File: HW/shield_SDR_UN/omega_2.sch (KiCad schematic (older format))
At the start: 15 parts

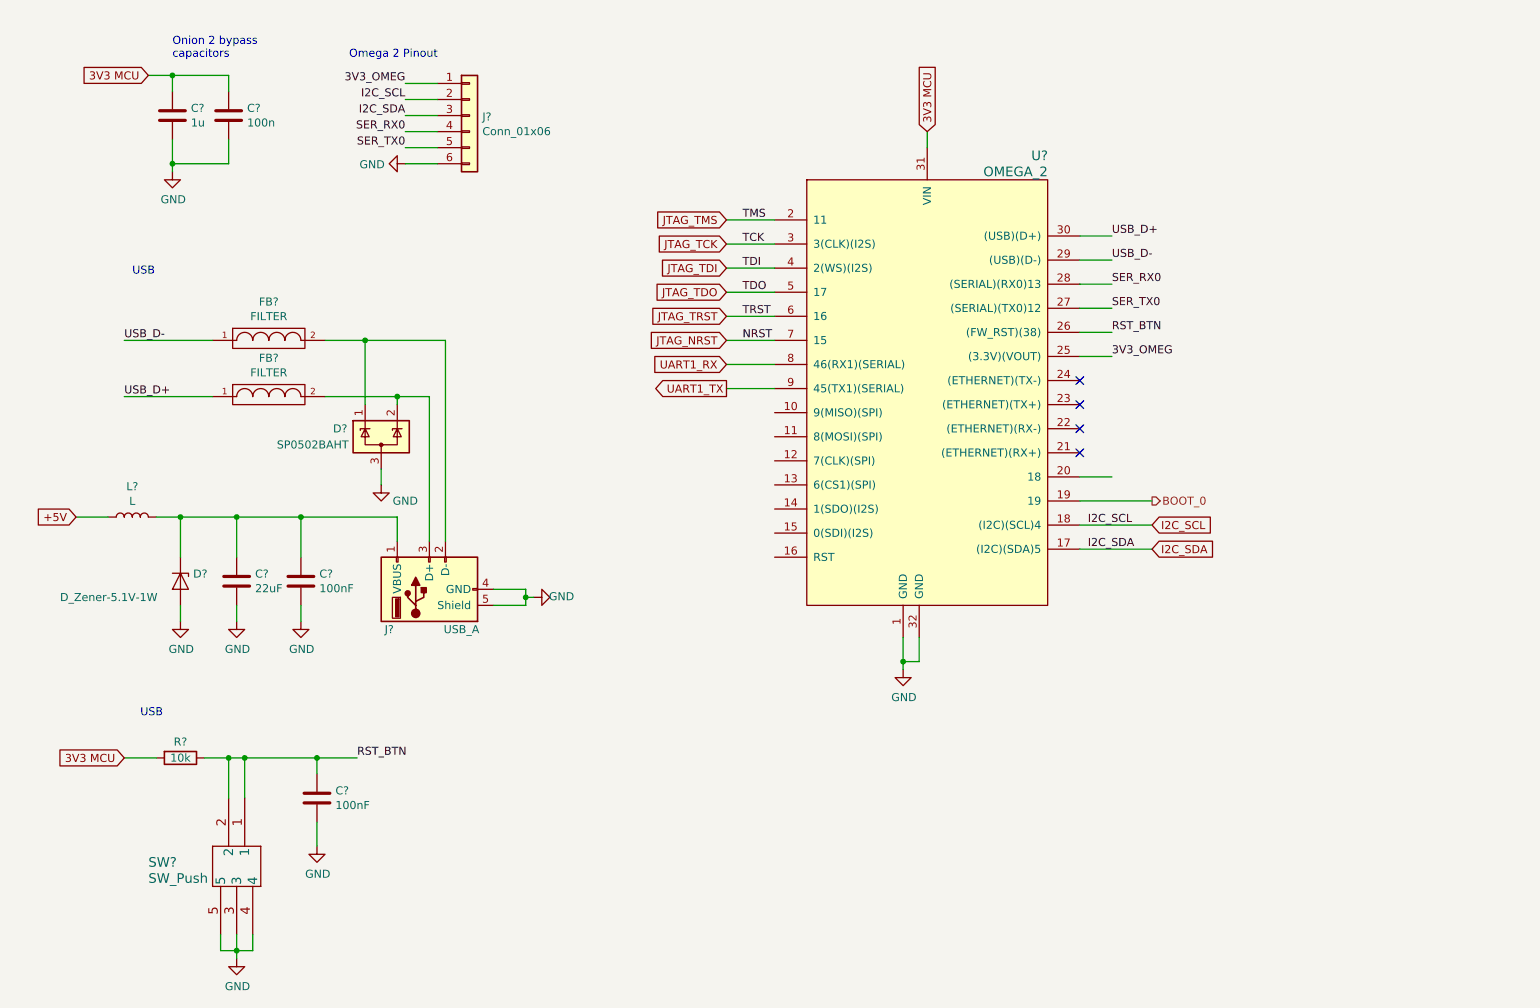
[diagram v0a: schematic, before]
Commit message: STM32 connection updated
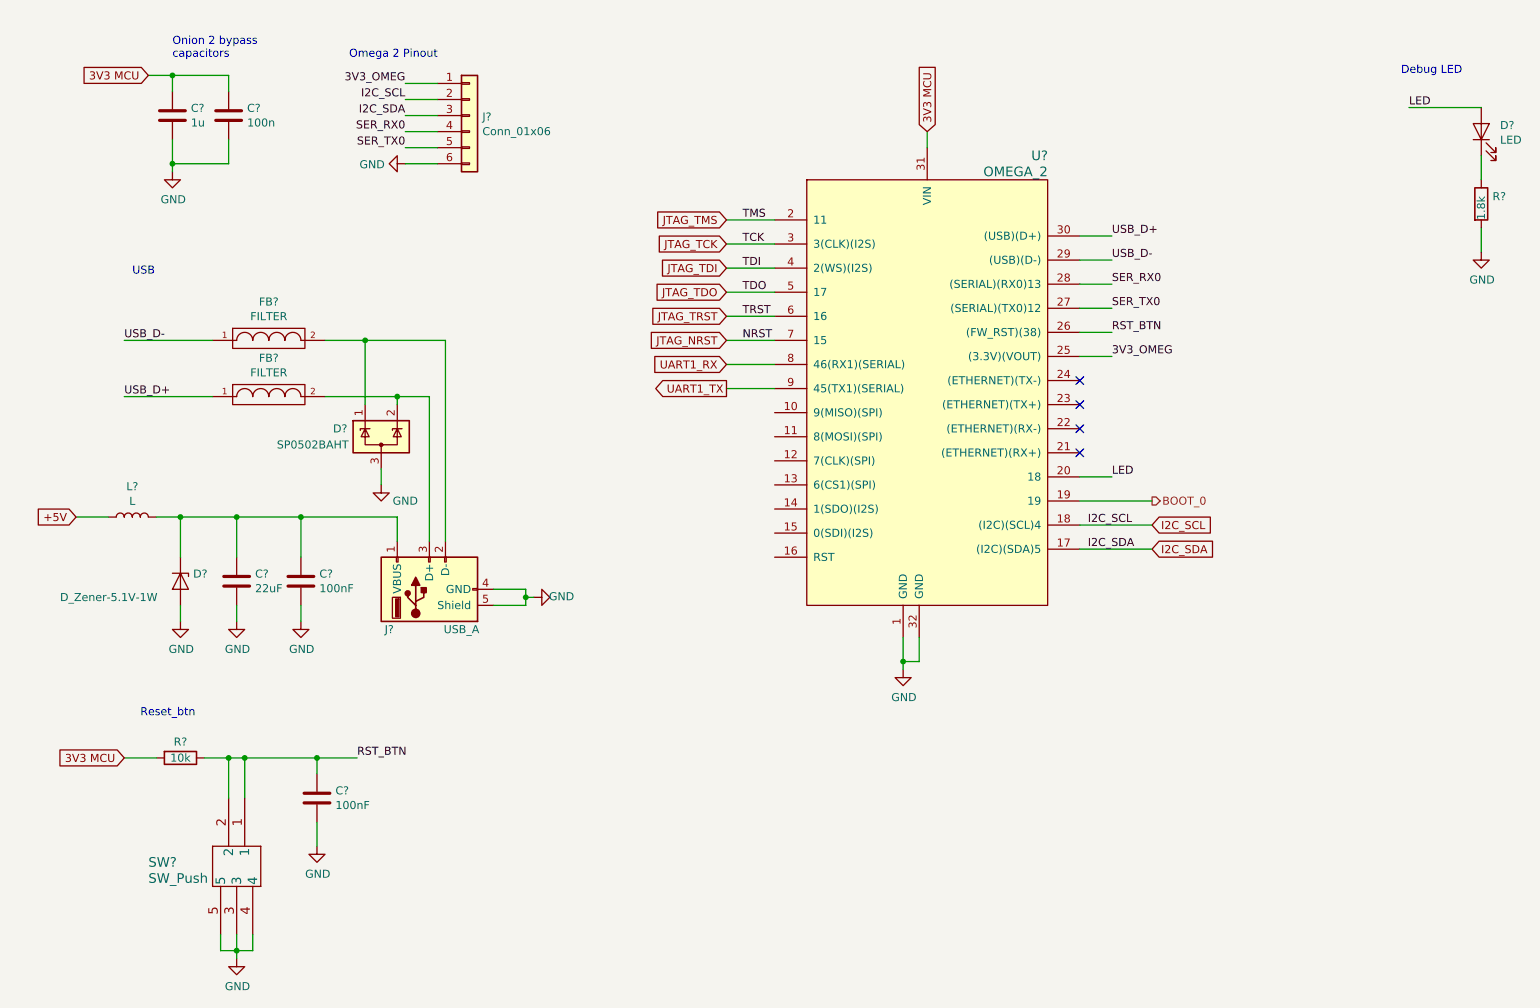
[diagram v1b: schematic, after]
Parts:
- added D?: LED, symbol Device:LED
- added R?: 1.8k, symbol Device:R
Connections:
- net GND: now also R?.2
- net LED: now reaches U?.20 (18)
- net LED: now also D?.2 (A)
- new net: D?.1 (K), R?.1
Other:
- note added: "Debug LED"
- note added: "Reset_btn"
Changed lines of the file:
@@
 RST_BTN
 Text Notes 1300 5050 0    50   ~ 0
-USB
+Reset_btn
 Wire Wire Line
 	5250 1950 4950 1950
@@
 Wire Wire Line
 	5250 3000 4950 3000
+$Comp
+L Device:LED D?
+U 1 1 5D35F1A3
+P 9650 1400
+AR Path="/5CC082AD/5D35F1A3" Ref="D?"  Part="1"
+AR Path="/5CFB52DC/5D35F1A3" Ref="D?"  Part="1"
+F 0 "D?" V 9689 1283 50  0000 R CNN
+F 1 "LED" V 9598 1283 50  0000 R CNN
+F 2 "" H 9650 1400 50  0001 C CNN
+F 3 "~" H 9650 1400 50  0001 C CNN
+	1    9650 1400
+	0    -1   -1   0
+$EndComp
+$Comp
+L Device:R R?
+U 1 1 5D35F1AD
+P 9650 1850
+AR Path="/5CC082AD/5D35F1AD" Ref="R?"  Part="1"
+AR Path="/5CFB52DC/5D35F1AD" Ref="R?"  Part="1"
+F 0 "R?" H 9720 1896 50  0000 L CNN
+F 1 "1.8k" V 9650 1750 50  0000 L CNN
+F 2 "" V 9580 1850 50  0001 C CNN
+F 3 "~" H 9650 1850 50  0001 C CNN
+	1    9650 1850
+	1    0    0    -1
+$EndComp
+$Comp
+L power:GND #PWR?
+U 1 1 5D35F1B5
+P 9650 2150
+F 0 "#PWR?" H 9650 1900 50  0001 C CNN
+F 1 "GND" H 9655 1977 50  0000 C CNN
+F 2 "" H 9650 2150 50  0001 C CNN
+F 3 "" H 9650 2150 50  0001 C CNN
+	1    9650 2150
+	1    0    0    -1
+$EndComp
+Wire Wire Line
+	9650 1250 9200 1250
+Wire Wire Line
+	9650 1550 9650 1700
+Wire Wire Line
+	9650 2000 9650 2150
+Text Label 9200 1250 0    50   ~ 0
+LED
+Text Notes 9150 1050 0    50   ~ 0
+Debug LED
+Text Label 7350 3550 0    50   ~ 0
+LED
 $EndSCHEMATC

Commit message: algunos footprint
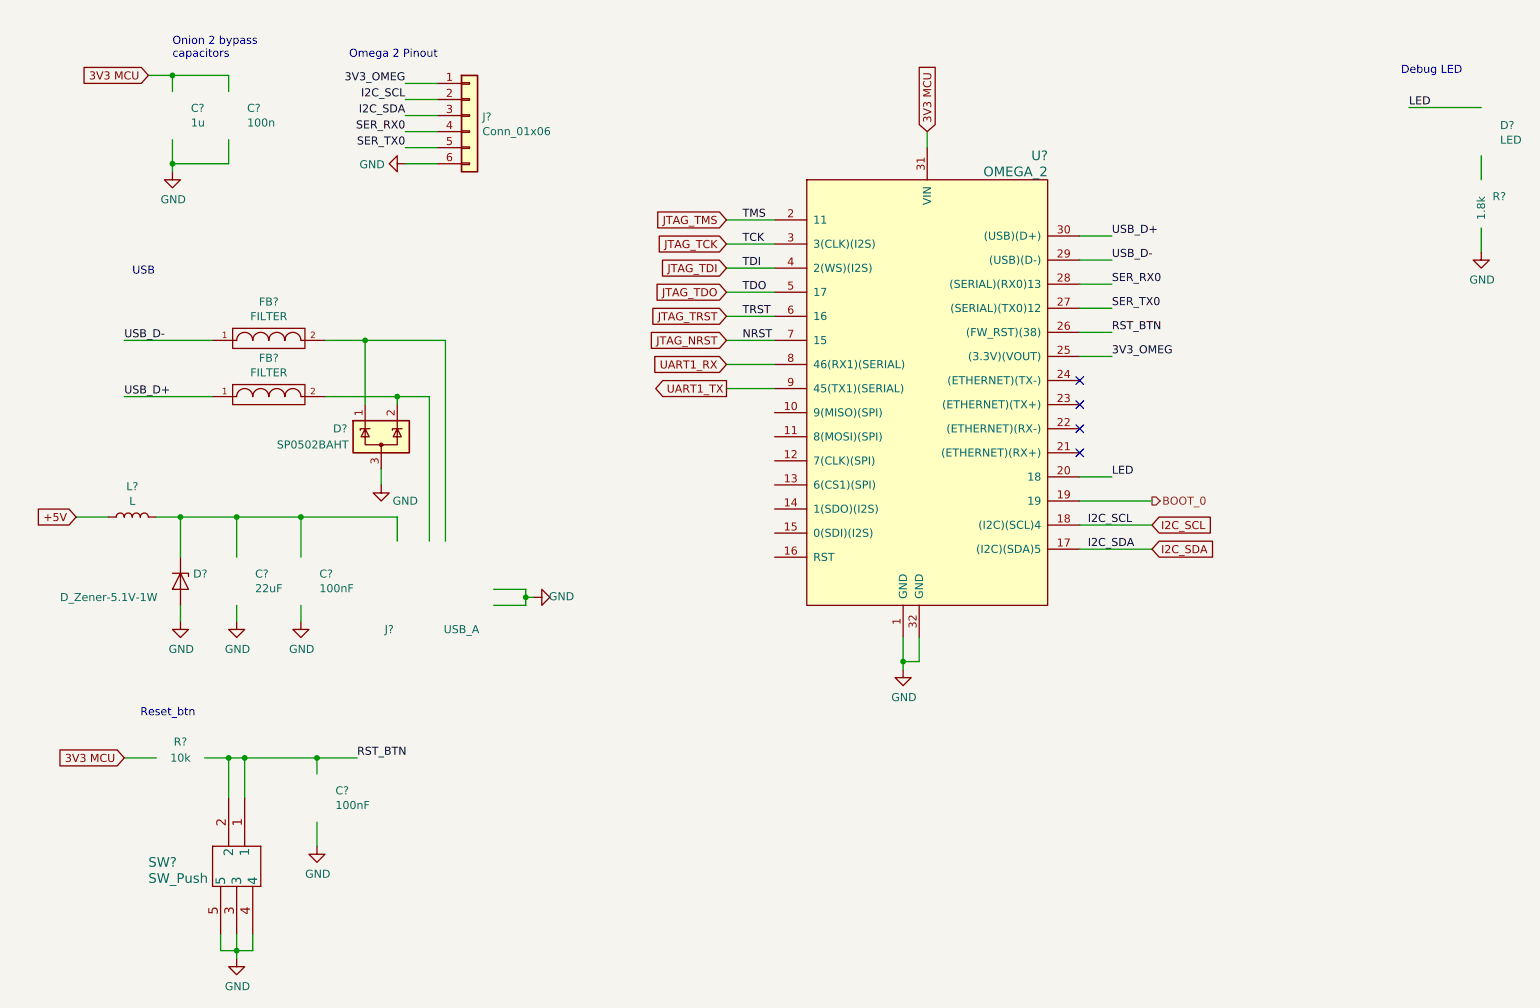
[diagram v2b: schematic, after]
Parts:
- C? (x2): footprint (none) -> Capacitor_SMD:C_0402_1005Metric
- D?: footprint (none) -> LED_SMD:LED_0805_2012Metric_Pad1.15x1.40mm_HandSolder
- J?: footprint (none) -> Connector_USB:USB_Micro-B_GCT_USB3076-30-A
- R? (x2): footprint (none) -> Resistor_SMD:R_0603_1608Metric_Pad1.05x0.95mm_HandSolder
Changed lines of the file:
@@
 $EndComp
 $Comp
-L power:GND #PWR?
+L power:GND #PWR0193
 U 1 1 5CE0713A
 P 6050 4750
-F 0 "#PWR?" H 6050 4500 50  0001 C CNN
+F 0 "#PWR0193" H 6050 4500 50  0001 C CNN
 F 1 "GND" H 6055 4577 50  0000 C CNN
 F 2 "" H 6050 4750 50  0001 C CNN
@@
 $Comp
 L Device:C C?
-U 1 1 5CE14EC4
+U 0 0 5CE14EC4
 P 1500 1300
 F 0 "C?" H 1615 1346 50  0000 L CNN
 F 1 "1u" H 1615 1255 50  0000 L CNN
-F 2 "" H 1538 1150 50  0001 C CNN
+F 2 "Capacitor_SMD:C_0402_1005Metric" H 1538 1150 50  0001 C CNN
 F 3 "~" H 1500 1300 50  0001 C CNN
-	1    1500 1300
+	0    1500 1300
 	1    0    0    -1
 $EndComp
 $Comp
 L Device:C C?
-U 1 1 5CE15558
+U 0 0 5CE15558
 P 1850 1300
 F 0 "C?" H 1965 1346 50  0000 L CNN
 F 1 "100n" H 1965 1255 50  0000 L CNN
-F 2 "" H 1888 1150 50  0001 C CNN
+F 2 "Capacitor_SMD:C_0402_1005Metric" H 1888 1150 50  0001 C CNN
 F 3 "~" H 1850 1300 50  0001 C CNN
-	1    1850 1300
-	1    0    0    -1
-$EndComp
-$Comp
-L power:GND #PWR?
+	0    1850 1300
+	1    0    0    -1
+$EndComp
+$Comp
+L power:GND #PWR0194
 U 1 1 5CE166D1
 P 1500 1650
-F 0 "#PWR?" H 1500 1400 50  0001 C CNN
+F 0 "#PWR0194" H 1500 1400 50  0001 C CNN
 F 1 "GND" H 1505 1477 50  0000 C CNN
 F 2 "" H 1500 1650 50  0001 C CNN
@@
 $Comp
 L Device:C C?
-U 1 1 5CECC457
+U 0 0 5CECC457
 P 1900 4200
 AR Path="/5CC08321/5CECC457" Ref="C?"  Part="1"
-AR Path="/5CFB52DC/5CECC457" Ref="C?"  Part="1"
+AR Path="/5CFB52DC/5CECC457" Ref="C?"  Part="0"
 F 0 "C?" H 2015 4246 50  0000 L CNN
 F 1 "22uF" H 2015 4155 50  0000 L CNN
 F 2 "modules:C_0805_HandSoldering" H 1938 4050 50  0001 C CNN
 F 3 "~" H 1900 4200 50  0001 C CNN
-	1    1900 4200
+	0    1900 4200
 	1    0    0    -1
 $EndComp
@@
 	3700 4250 3500 4250
 $Comp
-L power:GND #PWR?
+L power:GND #PWR0195
 U 1 1 5CECC493
 P 3750 4300
-F 0 "#PWR?" H 3750 4050 50  0001 C CNN
+F 0 "#PWR0195" H 3750 4050 50  0001 C CNN
 F 1 "GND" V 3755 4127 50  0000 C CNN
 F 2 "" H 3750 4300 50  0001 C CNN
@@
 $Comp
 L Device:C C?
-U 1 1 5CECC461
+U 0 0 5CECC461
 P 2300 4200
 AR Path="/5CC08321/5CECC461" Ref="C?"  Part="1"
-AR Path="/5CFB52DC/5CECC461" Ref="C?"  Part="1"
+AR Path="/5CFB52DC/5CECC461" Ref="C?"  Part="0"
 F 0 "C?" H 2415 4246 50  0000 L CNN
 F 1 "100nF" H 2415 4155 50  0000 L CNN
 F 2 "Capacitor_SMD:C_0402_1005Metric" H 2338 4050 50  0001 C CNN
 F 3 "~" H 2300 4200 50  0001 C CNN
-	1    2300 4200
-	1    0    0    -1
-$EndComp
-$Comp
-L power:GND #PWR?
+	0    2300 4200
+	1    0    0    -1
+$EndComp
+$Comp
+L power:GND #PWR0196
 U 1 1 5CF38DF9
 P 1900 4450
-F 0 "#PWR?" H 1900 4200 50  0001 C CNN
+F 0 "#PWR0196" H 1900 4200 50  0001 C CNN
 F 1 "GND" H 1905 4277 50  0000 C CNN
 F 2 "" H 1900 4450 50  0001 C CNN
@@
 $EndComp
 $Comp
-L power:GND #PWR?
+L power:GND #PWR0197
 U 1 1 5CF3BDF7
 P 2300 4450
-F 0 "#PWR?" H 2300 4200 50  0001 C CNN
+F 0 "#PWR0197" H 2300 4200 50  0001 C CNN
 F 1 "GND" H 2305 4277 50  0000 C CNN
 F 2 "" H 2300 4450 50  0001 C CNN
@@
 $EndComp
 $Comp
-L power:GND #PWR?
+L power:GND #PWR0198
 U 1 1 5CF3C29A
 P 1550 4450
-F 0 "#PWR?" H 1550 4200 50  0001 C CNN
+F 0 "#PWR0198" H 1550 4200 50  0001 C CNN
 F 1 "GND" H 1555 4277 50  0000 C CNN
 F 2 "" H 1550 4450 50  0001 C CNN
@@
 $Comp
 L Connector:USB_A J?
-U 1 1 5CECC443
+U 0 0 5CECC443
 P 3100 4250
 AR Path="/5CC08321/5CECC443" Ref="J?"  Part="1"
-AR Path="/5CFB52DC/5CECC443" Ref="J?"  Part="1"
+AR Path="/5CFB52DC/5CECC443" Ref="J?"  Part="0"
 F 0 "J?" V 2850 4500 50  0000 C CNN
 F 1 "USB_A" V 2850 4050 50  0000 C CNN
-F 2 "" H 3250 4200 50  0001 C CNN
+F 2 "Connector_USB:USB_Micro-B_GCT_USB3076-30-A" H 3250 4200 50  0001 C CNN
 F 3 "" H 3250 4200 50  0001 C CNN
 F 4 "https://www.digikey.com/product-detail/en/amphenol-icc-commercial-products/UE27AC54100/UE27AC54100-ND/1972253" H 3100 4250 50  0001 C CNN "digikey"
-	1    3100 4250
+	0    3100 4250
 	0    -1   -1   0
 $EndComp
@@
 $EndComp
 $Comp
-L power:GND #PWR?
+L power:GND #PWR0199
 U 1 1 5CF9308C
 P 2800 3600
-F 0 "#PWR?" H 2800 3350 50  0001 C CNN
+F 0 "#PWR0199" H 2800 3350 50  0001 C CNN
 F 1 "GND" H 2950 3500 50  0000 C CNN
 F 2 "" H 2800 3600 50  0001 C CNN
@@
 3V3_OMEG
 $Comp
-L power:GND #PWR?
+L power:GND #PWR0200
 U 1 1 5D026364
 P 2950 1600
-F 0 "#PWR?" H 2950 1350 50  0001 C CNN
+F 0 "#PWR0200" H 2950 1350 50  0001 C CNN
 F 1 "GND" V 2955 1472 50  0000 R CNN
 F 2 "" H 2950 1600 50  0001 C CNN
@@
 $Comp
 L Device:R R?
-U 1 1 5CD67141
+U 0 0 5CD67141
 P 1550 5300
 F 0 "R?" V 1450 5300 50  0000 C CNN
 F 1 "10k" V 1550 5300 50  0000 C CNN
-F 2 "" V 1480 5300 50  0001 C CNN
+F 2 "Resistor_SMD:R_0603_1608Metric_Pad1.05x0.95mm_HandSolder" V 1480 5300 50  0001 C CNN
 F 3 "~" H 1550 5300 50  0001 C CNN
-	1    1550 5300
+	0    1550 5300
 	0    1    1    0
 $EndComp
@@
 	1400 5300 1200 5300
 $Comp
-L power:GND #PWR?
+L power:GND #PWR0201
 U 1 1 5CD80A5F
 P 1900 6550
-F 0 "#PWR?" H 1900 6300 50  0001 C CNN
+F 0 "#PWR0201" H 1900 6300 50  0001 C CNN
 F 1 "GND" H 1905 6377 50  0000 C CNN
 F 2 "" H 1900 6550 50  0001 C CNN
@@
 $Comp
 L Device:C C?
-U 1 1 5CD83476
+U 0 0 5CD83476
 P 2400 5550
 AR Path="/5CC08321/5CD83476" Ref="C?"  Part="1"
-AR Path="/5CFB52DC/5CD83476" Ref="C?"  Part="1"
+AR Path="/5CFB52DC/5CD83476" Ref="C?"  Part="0"
 F 0 "C?" H 2515 5596 50  0000 L CNN
 F 1 "100nF" H 2515 5505 50  0000 L CNN
 F 2 "Capacitor_SMD:C_0402_1005Metric" H 2438 5400 50  0001 C CNN
 F 3 "~" H 2400 5550 50  0001 C CNN
-	1    2400 5550
-	1    0    0    -1
-$EndComp
-$Comp
-L power:GND #PWR?
+	0    2400 5550
+	1    0    0    -1
+$EndComp
+$Comp
+L power:GND #PWR0202
 U 1 1 5CD83F6F
 P 2400 5850
-F 0 "#PWR?" H 2400 5600 50  0001 C CNN
+F 0 "#PWR0202" H 2400 5600 50  0001 C CNN
 F 1 "GND" H 2405 5677 50  0000 C CNN
 F 2 "" H 2400 5850 50  0001 C CNN
@@
 $Comp
 L Device:LED D?
-U 1 1 5D35F1A3
+U 0 0 5D35F1A3
 P 9650 1400
 AR Path="/5CC082AD/5D35F1A3" Ref="D?"  Part="1"
-AR Path="/5CFB52DC/5D35F1A3" Ref="D?"  Part="1"
+AR Path="/5CFB52DC/5D35F1A3" Ref="D?"  Part="0"
 F 0 "D?" V 9689 1283 50  0000 R CNN
 F 1 "LED" V 9598 1283 50  0000 R CNN
-F 2 "" H 9650 1400 50  0001 C CNN
+F 2 "LED_SMD:LED_0805_2012Metric_Pad1.15x1.40mm_HandSolder" H 9650 1400 50  0001 C CNN
 F 3 "~" H 9650 1400 50  0001 C CNN
-	1    9650 1400
+	0    9650 1400
 	0    -1   -1   0
 $EndComp
 $Comp
 L Device:R R?
-U 1 1 5D35F1AD
+U 0 0 5D35F1AD
 P 9650 1850
 AR Path="/5CC082AD/5D35F1AD" Ref="R?"  Part="1"
-AR Path="/5CFB52DC/5D35F1AD" Ref="R?"  Part="1"
+AR Path="/5CFB52DC/5D35F1AD" Ref="R?"  Part="0"
 F 0 "R?" H 9720 1896 50  0000 L CNN
 F 1 "1.8k" V 9650 1750 50  0000 L CNN
-F 2 "" V 9580 1850 50  0001 C CNN
+F 2 "Resistor_SMD:R_0603_1608Metric_Pad1.05x0.95mm_HandSolder" V 9580 1850 50  0001 C CNN
 F 3 "~" H 9650 1850 50  0001 C CNN
-	1    9650 1850
-	1    0    0    -1
-$EndComp
-$Comp
-L power:GND #PWR?
+	0    9650 1850
+	1    0    0    -1
+$EndComp
+$Comp
+L power:GND #PWR0203
 U 1 1 5D35F1B5
 P 9650 2150
-F 0 "#PWR?" H 9650 1900 50  0001 C CNN
+F 0 "#PWR0203" H 9650 1900 50  0001 C CNN
 F 1 "GND" H 9655 1977 50  0000 C CNN
 F 2 "" H 9650 2150 50  0001 C CNN

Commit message: algunos footprint_v2
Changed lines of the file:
@@
 $Comp
 L Device:C C?
-U 0 0 5CE14EC4
+U 1 1 5CE14EC4
 P 1500 1300
 F 0 "C?" H 1615 1346 50  0000 L CNN
@@
 F 2 "Capacitor_SMD:C_0402_1005Metric" H 1538 1150 50  0001 C CNN
 F 3 "~" H 1500 1300 50  0001 C CNN
-	0    1500 1300
+	1    1500 1300
 	1    0    0    -1
 $EndComp
 $Comp
 L Device:C C?
-U 0 0 5CE15558
+U 1 1 5CE15558
 P 1850 1300
 F 0 "C?" H 1965 1346 50  0000 L CNN
@@
 F 2 "Capacitor_SMD:C_0402_1005Metric" H 1888 1150 50  0001 C CNN
 F 3 "~" H 1850 1300 50  0001 C CNN
-	0    1850 1300
+	1    1850 1300
 	1    0    0    -1
 $EndComp
@@
 $Comp
 L Device:C C?
-U 0 0 5CECC457
+U 1 1 5CECC457
 P 1900 4200
 AR Path="/5CC08321/5CECC457" Ref="C?"  Part="1"
@@
 F 2 "modules:C_0805_HandSoldering" H 1938 4050 50  0001 C CNN
 F 3 "~" H 1900 4200 50  0001 C CNN
-	0    1900 4200
+	1    1900 4200
 	1    0    0    -1
 $EndComp
@@
 $Comp
 L Device:C C?
-U 0 0 5CECC461
+U 1 1 5CECC461
 P 2300 4200
 AR Path="/5CC08321/5CECC461" Ref="C?"  Part="1"
@@
 F 2 "Capacitor_SMD:C_0402_1005Metric" H 2338 4050 50  0001 C CNN
 F 3 "~" H 2300 4200 50  0001 C CNN
-	0    2300 4200
+	1    2300 4200
 	1    0    0    -1
 $EndComp
@@
 $Comp
 L Connector:USB_A J?
-U 0 0 5CECC443
+U 1 1 5CECC443
 P 3100 4250
 AR Path="/5CC08321/5CECC443" Ref="J?"  Part="1"
@@
 F 3 "" H 3250 4200 50  0001 C CNN
 F 4 "https://www.digikey.com/product-detail/en/amphenol-icc-commercial-products/UE27AC54100/UE27AC54100-ND/1972253" H 3100 4250 50  0001 C CNN "digikey"
-	0    3100 4250
+	1    3100 4250
 	0    -1   -1   0
 $EndComp
@@
 $Comp
 L Device:R R?
-U 0 0 5CD67141
+U 1 1 5CD67141
 P 1550 5300
 F 0 "R?" V 1450 5300 50  0000 C CNN
@@
 F 2 "Resistor_SMD:R_0603_1608Metric_Pad1.05x0.95mm_HandSolder" V 1480 5300 50  0001 C CNN
 F 3 "~" H 1550 5300 50  0001 C CNN
-	0    1550 5300
+	1    1550 5300
 	0    1    1    0
 $EndComp
@@
 $Comp
 L Device:C C?
-U 0 0 5CD83476
+U 1 1 5CD83476
 P 2400 5550
 AR Path="/5CC08321/5CD83476" Ref="C?"  Part="1"
@@
 F 2 "Capacitor_SMD:C_0402_1005Metric" H 2438 5400 50  0001 C CNN
 F 3 "~" H 2400 5550 50  0001 C CNN
-	0    2400 5550
+	1    2400 5550
 	1    0    0    -1
 $EndComp
@@
 $Comp
 L Device:LED D?
-U 0 0 5D35F1A3
+U 1 1 5D35F1A3
 P 9650 1400
 AR Path="/5CC082AD/5D35F1A3" Ref="D?"  Part="1"
@@
 F 2 "LED_SMD:LED_0805_2012Metric_Pad1.15x1.40mm_HandSolder" H 9650 1400 50  0001 C CNN
 F 3 "~" H 9650 1400 50  0001 C CNN
-	0    9650 1400
+	1    9650 1400
 	0    -1   -1   0
 $EndComp
 $Comp
 L Device:R R?
-U 0 0 5D35F1AD
+U 1 1 5D35F1AD
 P 9650 1850
 AR Path="/5CC082AD/5D35F1AD" Ref="R?"  Part="1"
@@
 F 2 "Resistor_SMD:R_0603_1608Metric_Pad1.05x0.95mm_HandSolder" V 9580 1850 50  0001 C CNN
 F 3 "~" H 9650 1850 50  0001 C CNN
-	0    9650 1850
-	1    0    0    -1
-$EndComp
+	1    9650 1850
+	1    0    0    -1
+$EndComp
